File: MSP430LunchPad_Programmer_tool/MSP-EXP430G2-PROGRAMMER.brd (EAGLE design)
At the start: 50.8 x 48.3 mm, 6 parts

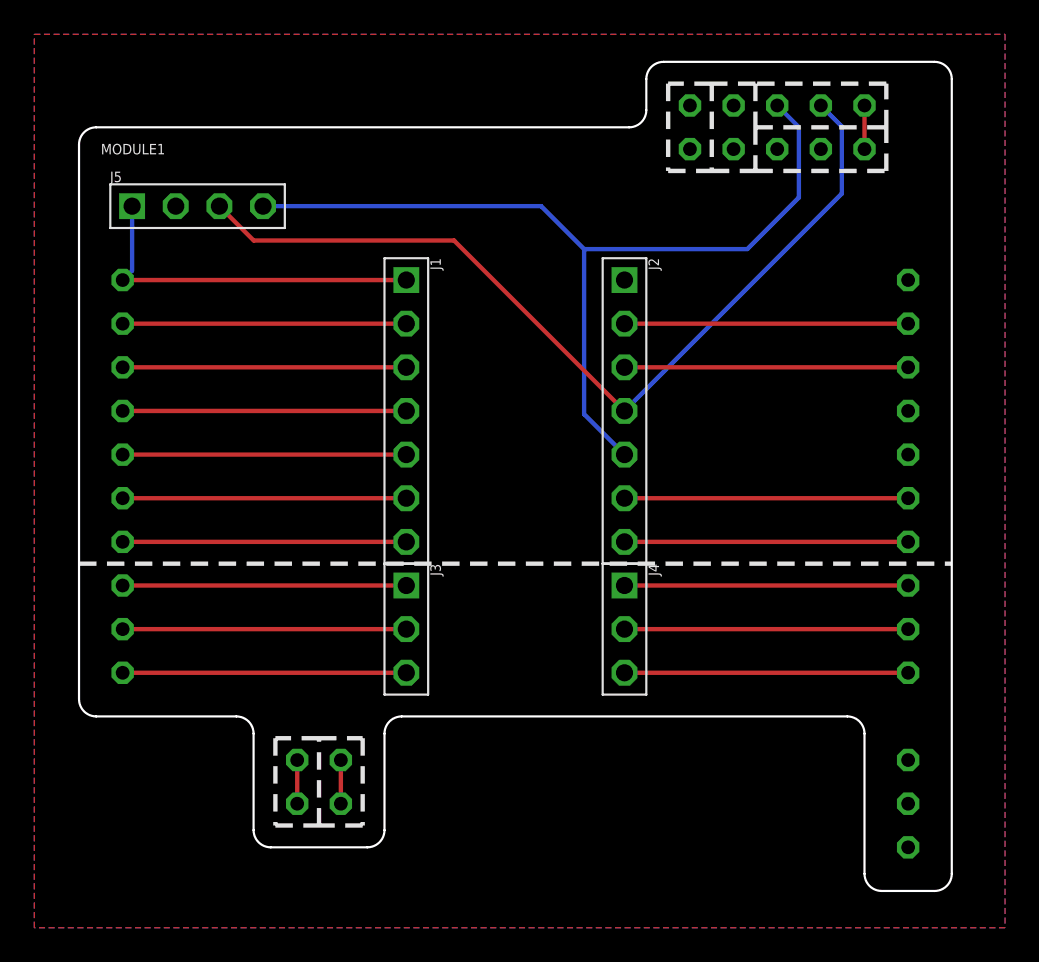
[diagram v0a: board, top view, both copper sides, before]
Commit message: launchpad programmer done
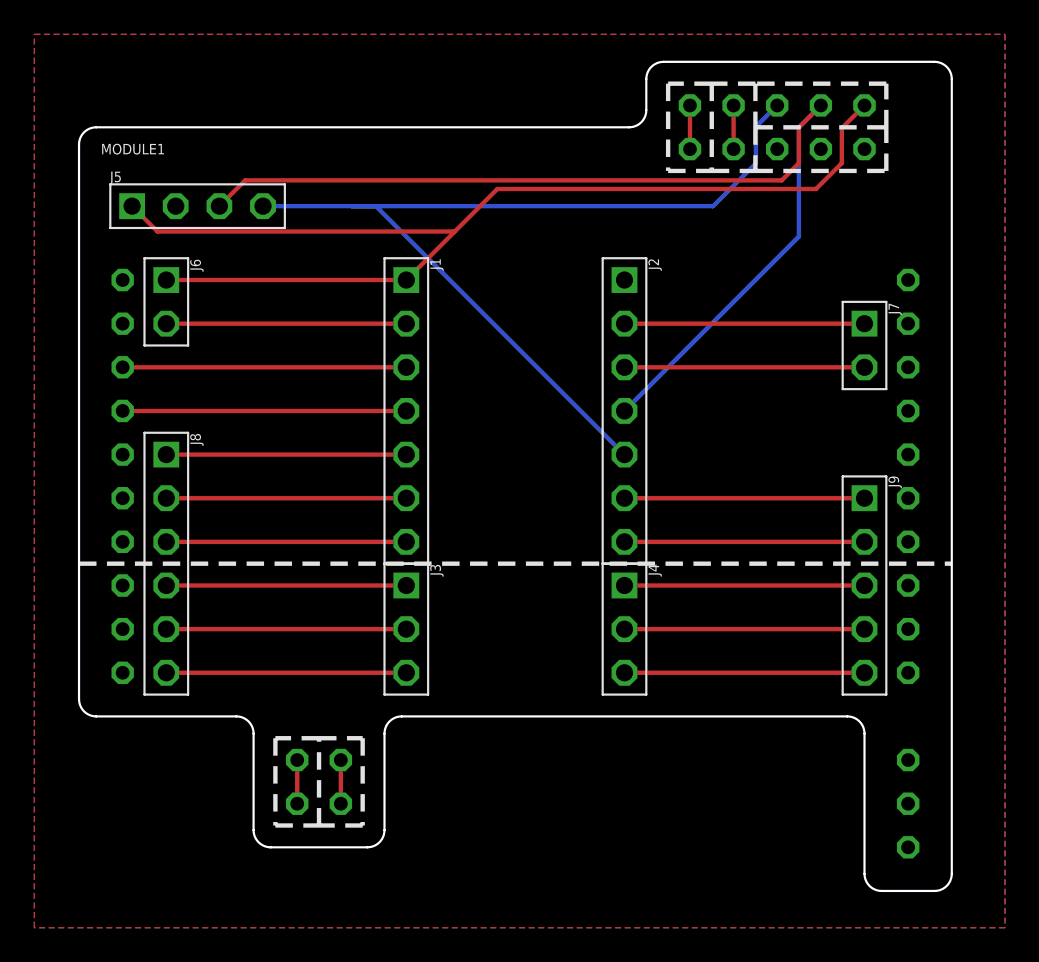
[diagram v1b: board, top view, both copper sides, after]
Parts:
- added J6, J7: (no value), Connectors:2PIN_HEADER_PITCH2.54MM_TH
- added J8: (no value), Connectors:6PIN_HEADER_PITCH2.54MM_TH
- added J9: (no value), Connectors:5PIN_HEADER_PITCH2.54MM_TH
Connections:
- net N$12 renamed RESET
- net N$8 renamed TEST
- removed net N$19: J4.1, MODULE1.P2.5
- removed net N$20: J4.3, MODULE1.P2.3
- removed net N$26: MODULE1.VCC, MODULE1.VCC1
- new net N$11: J3.3, J8.6
- new net N$12: J2.2, J7.1
- new net N$8: J1.7, J8.3
- new net VCC: J1.1, J5.1, J6.1, MODULE1.VCC
- net N$10: now also J3.2, J8.5; no longer J2.2, MODULE1.XIN
- net N$13: now also J2.3, J7.2; no longer J2.6, MODULE1.P1.7
- net N$14: now also J2.6, J9.1; no longer J2.7, MODULE1.P1.6
- net N$15: now also J2.7, J9.2; no longer J3.2, MODULE1.P2.1
- net N$16: now also J4.1, J9.3; no longer J3.1, MODULE1.P2.0
- net N$17: now also J4.2, J9.4; no longer J3.3, MODULE1.P2.2
- net N$18: now also J4.3, J9.5; no longer J4.2, MODULE1.P2.4
- net N$3: now also MODULE1.P1.1-1, MODULE1.TX; no longer J1.2, MODULE1.P1.0
- net N$4: now also MODULE1.P1.2-1, MODULE1.RX; no longer J1.1, J5.1, MODULE1.VCC2
- net N$5: now also J1.2, J6.2; no longer J1.5, MODULE1.P1.3
- net N$6: now also J1.5, J8.1; no longer J1.6, MODULE1.P1.4
- net N$7: now also J1.6, J8.2; no longer J1.7, MODULE1.P1.5
- net N$9: now also J3.1, J8.4; no longer J2.3, MODULE1.XOUT
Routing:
- net VCC: track 0.00 -> 65.4 mm
- net N$4: track 21.0 -> 2.54 mm
- net N$20: track 16.5 -> 0.00 mm
- net N$19: track 16.5 -> 0.00 mm
- net N$8: track 0.00 -> 14.0 mm
- net N$12: track 0.00 -> 14.0 mm
- net N$11: track 0.00 -> 14.0 mm
- net N$3: track 16.5 -> 2.54 mm
- net TEST: track 52.0 -> 61.2 mm
- net RESET: track 52.3 -> 55.4 mm
- net N$26: track 2.54 -> 0.00 mm
- net N$9: track 16.5 -> 14.0 mm
- net N$7: track 16.5 -> 14.0 mm
- net N$6: track 16.5 -> 14.0 mm
- net N$5: track 16.5 -> 14.0 mm
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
